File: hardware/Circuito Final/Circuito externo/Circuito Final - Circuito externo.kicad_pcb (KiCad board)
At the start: 2 copper layers, 124.6 x 134.4 mm, 81 parts, among them J1 Conn_02x19_Odd_Even, J2 Conn_02x19_Odd_Even, J3 Conn_01x02, J4 Conn_01x02, J5 Conn_01x03_Pin, J6 Conn_01x03_Pin, Q1 FDMS6681Z, Q2 FDMS6681Z, Q3 MMBT2222A, SW1 SW_SPDT, SW2 SW_DIP_x04, SW3 SW_DIP_x04, SW4 SW_DIP_x01, SW5 SW_DIP_x01, SW6 SW_DIP_x01, U1 Opamp_Quad, U2 ICL7660, U3 INA180A1, U4 INA180A1

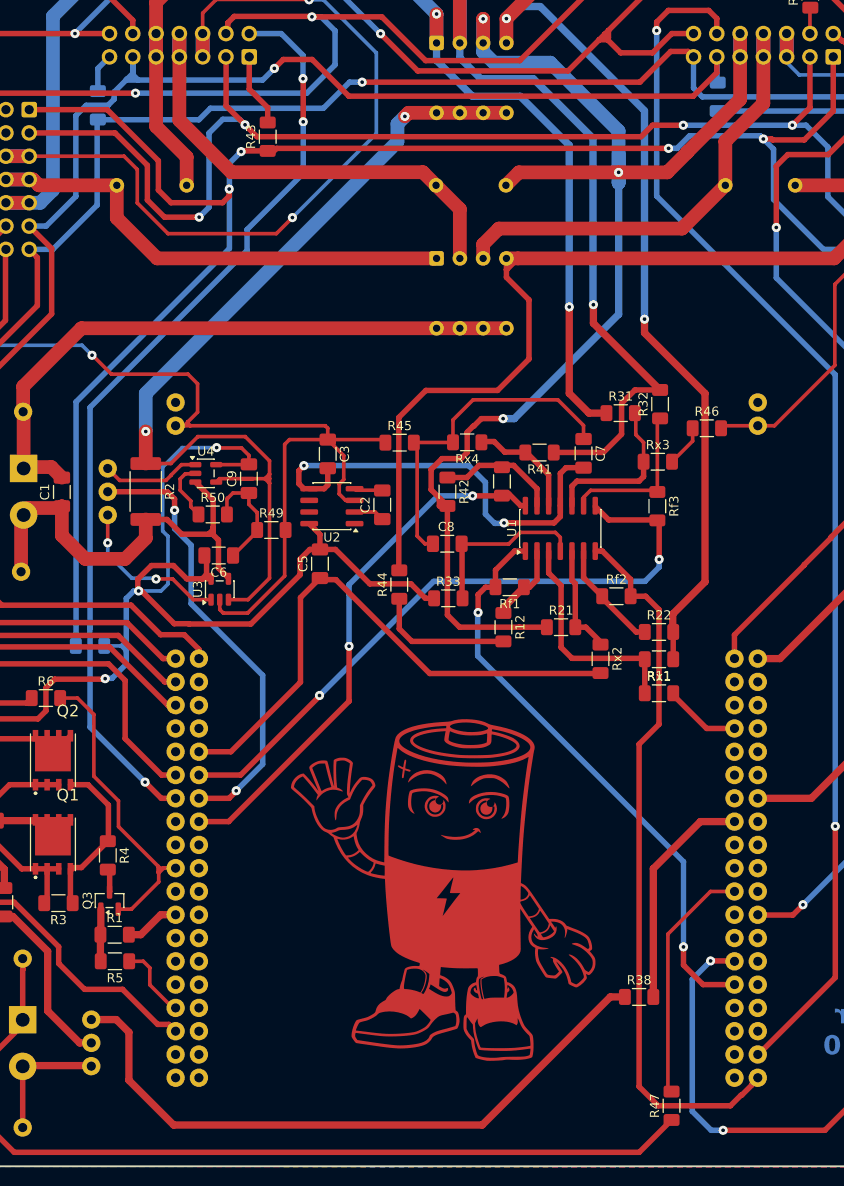
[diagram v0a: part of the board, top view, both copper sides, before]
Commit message: toma ambas mediciones de los ina con la stm
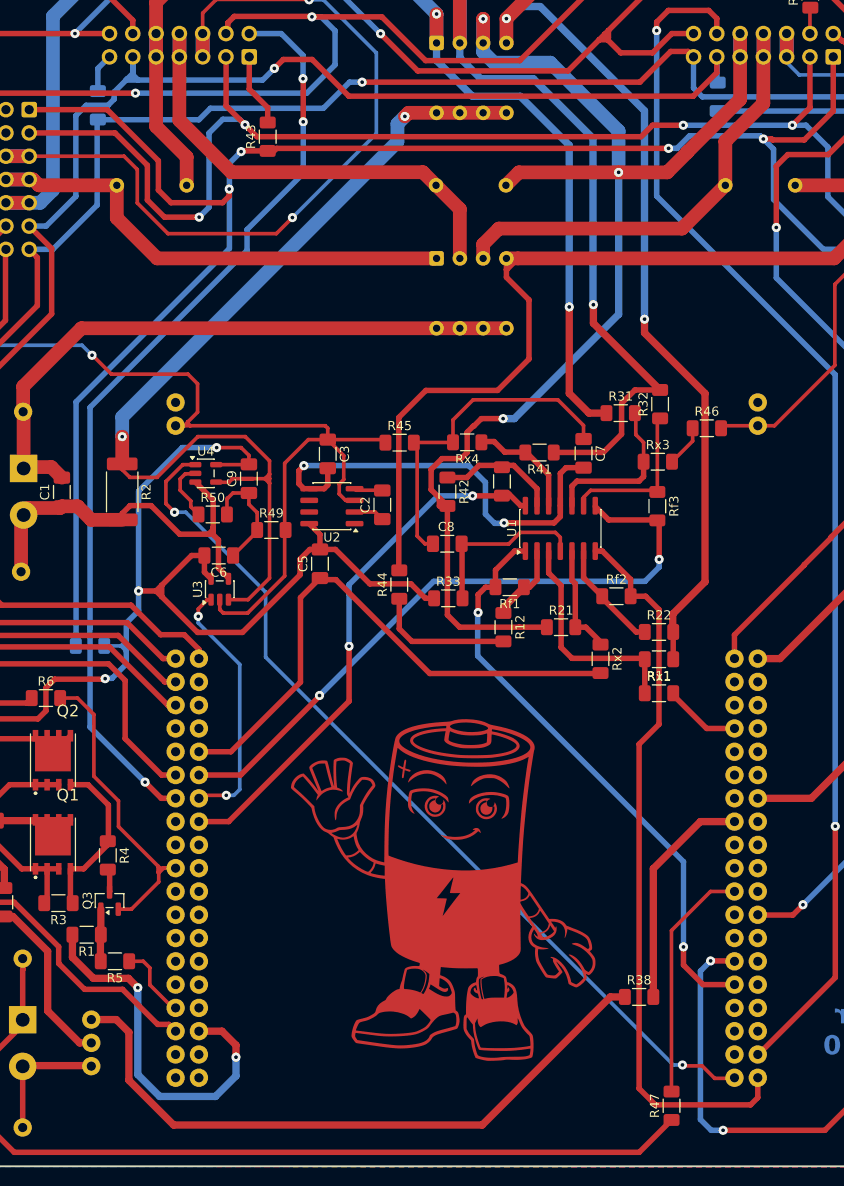
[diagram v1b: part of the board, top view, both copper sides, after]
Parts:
- removed J6: Conn_01x03_Pin, Connector_PinHeader_2.54mm:PinHeader_1x03_P2.54mm_Vertical
- moved R1 3.06 mm to (57.9, 149.3), turned to 180 degrees
- moved R2 2.57 mm to (61.7, 101.0)
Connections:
- J1 pad 37: unconnected-(J1-Pin_37-Pad37) -> /medicion_corriente_de_carga
- J2 pad 14: /medicion_corriente -> /medicion_corriente_de_descarga
- J2 pad 23: /llave_de_emergencia -> unconnected-(J2-Pin_23-Pad23)
- J2 pad 34: unconnected-(J2-Pin_34-Pad34) -> /llave_de_emergencia
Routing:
- net /medicion_corriente_de_carga: track 10.8 -> 98.5 mm, vias 0 -> 2
- net /medicion_corriente: track 49.1 -> 0.00 mm, vias 2 -> 0
- net /llave_de_emergencia: track 6.00 -> 41.1 mm, vias 0 -> 2
- net /medicion_corriente_de_descarga: track 17.6 -> 27.8 mm
- net /bus_pos_salida: track 103.4 -> 108.7 mm
- net /shunt: track 48.2 -> 43.3 mm
- net /bus_pos_2: track 146.5 -> 142.2 mm
- net /Vcc_out: track 316.8 -> 312.5 mm
- net GND: track 575.4 -> 573.5 mm
- net /banco2_med: track 78.7 -> 79.9 mm
- net /salida_adc_1: track 152.7 -> 151.9 mm

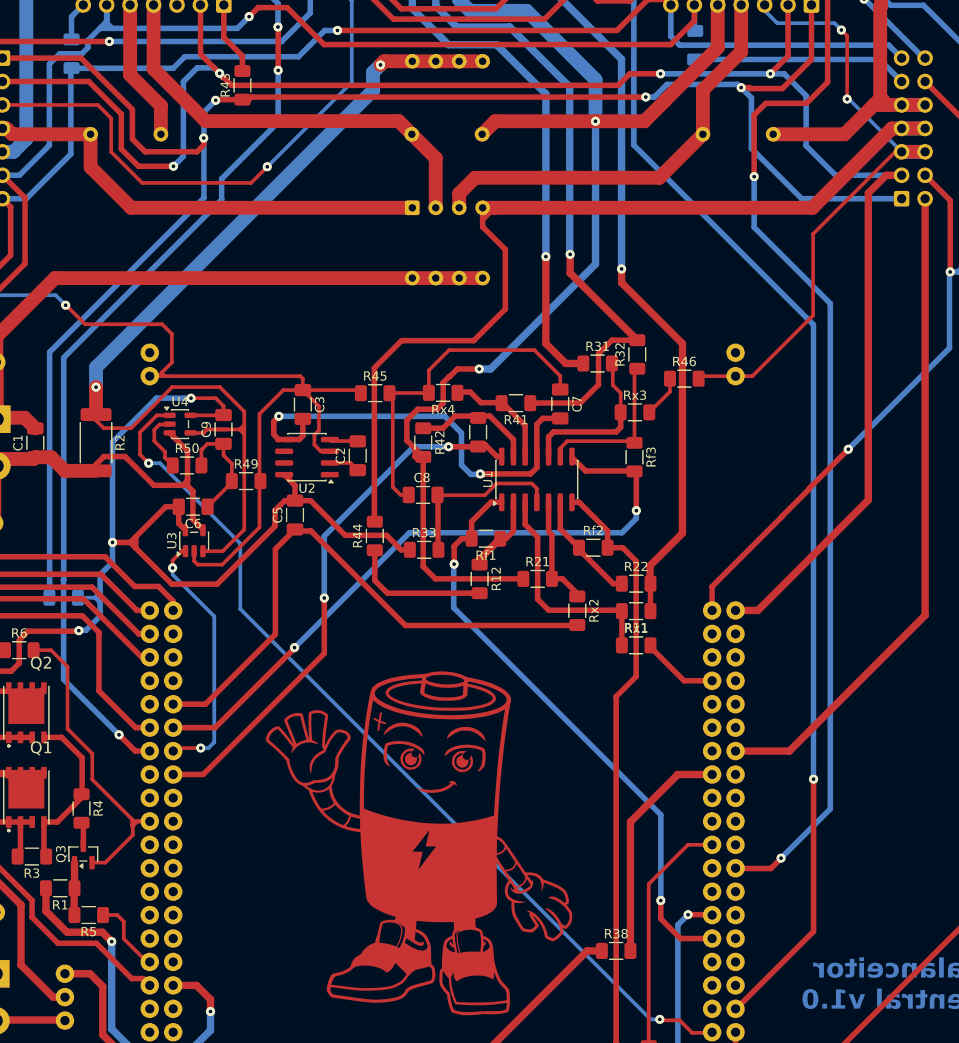
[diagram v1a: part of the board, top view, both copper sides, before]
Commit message: acomoda un par de pistas
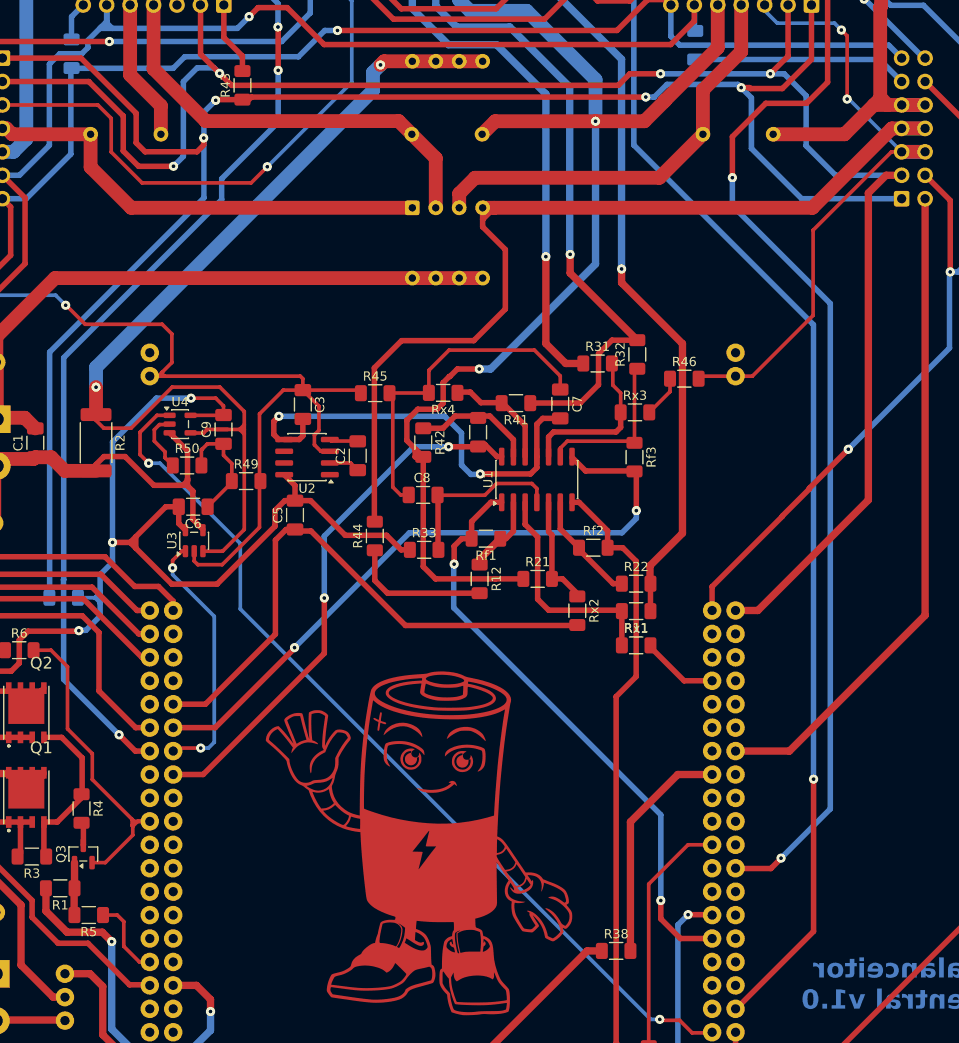
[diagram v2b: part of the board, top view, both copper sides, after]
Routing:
- net /Data_2: track 112.7 -> 114.6 mm
- net GND: track 573.5 -> 574.7 mm

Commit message: agrega lagrima faltante
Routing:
- net GND: track 574.7 -> 573.4 mm

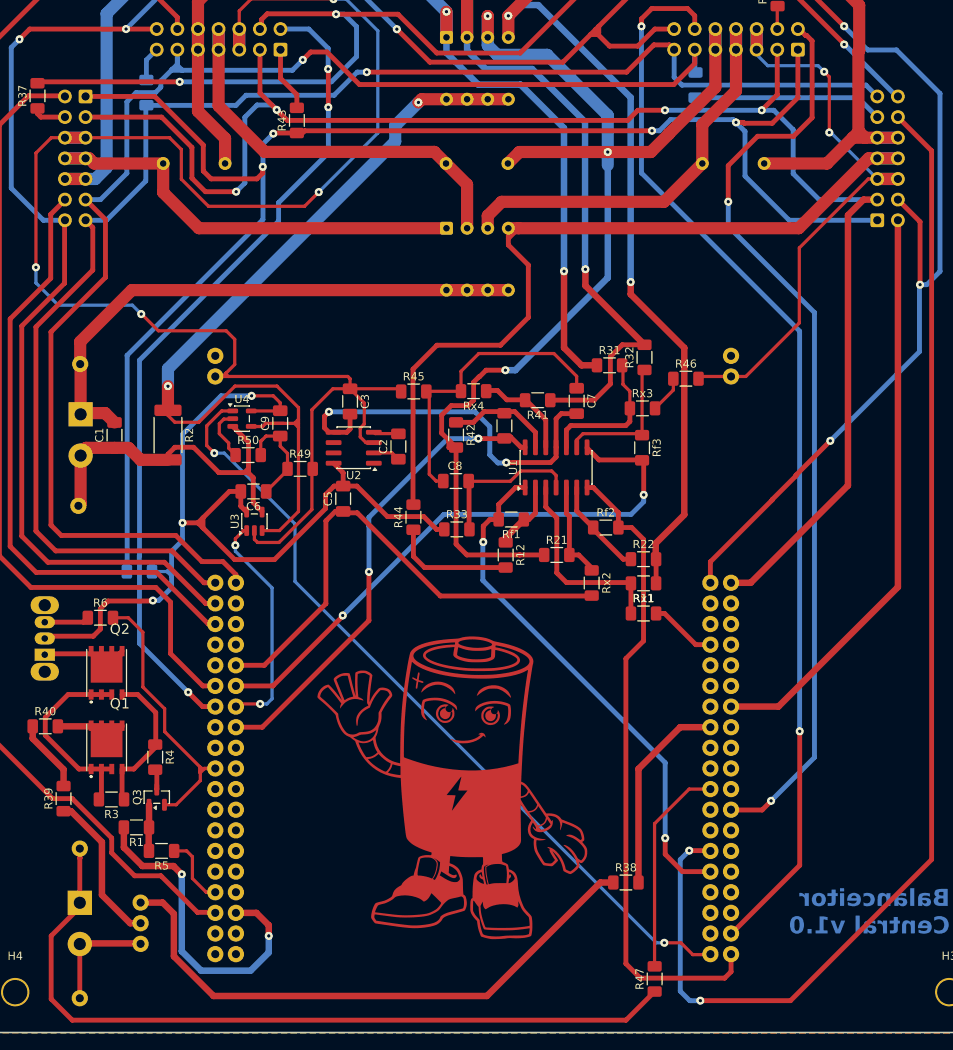
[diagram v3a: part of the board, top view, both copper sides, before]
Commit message: conecta los gnd de la stm
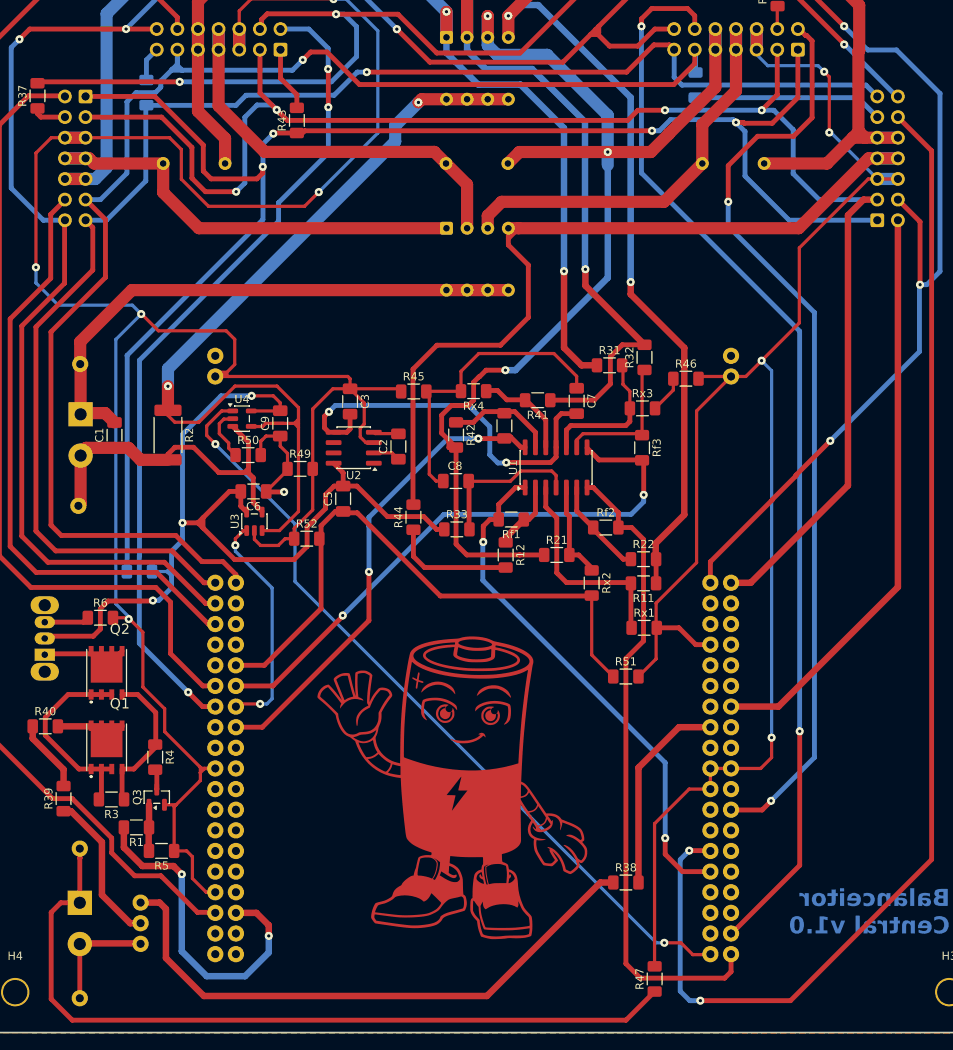
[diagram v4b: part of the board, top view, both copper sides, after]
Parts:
- added R51: 0, Resistor_SMD:R_1206_3216Metric_Pad1.30x1.75mm_HandSolder, F.Cu at (118.1, 130.8)
- added R52: 0, Resistor_SMD:R_1206_3216Metric_Pad1.30x1.75mm_HandSolder, F.Cu at (78.8, 113.8)
- moved Rx1 1.77 mm to (120.4, 124.8)
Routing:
- net GND: track 573.4 -> 736.8 mm, vias 6 -> 10
- net Net-(U1A-+): track 24.3 -> 26.0 mm
- net /Vcc_out: track 312.5 -> 313.9 mm
- net /medicion_corriente_de_carga: track 98.5 -> 97.7 mm
- net /Vcc_neg: track 47.4 -> 48.1 mm
- net /Vcc_stm: track 96.8 -> 97.3 mm
- net /llave_de_emergencia: track 41.1 -> 41.7 mm
